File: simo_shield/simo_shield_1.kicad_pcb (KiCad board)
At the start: 2 copper layers, 70 x 100 mm, 10 parts, among them J1 modulo_usb_debug, J2 conector_bateria, U1 elemon_board, U2 modulo_flash_externa, U3 bluepill_board_stm32, U4 modulo_acelerometro

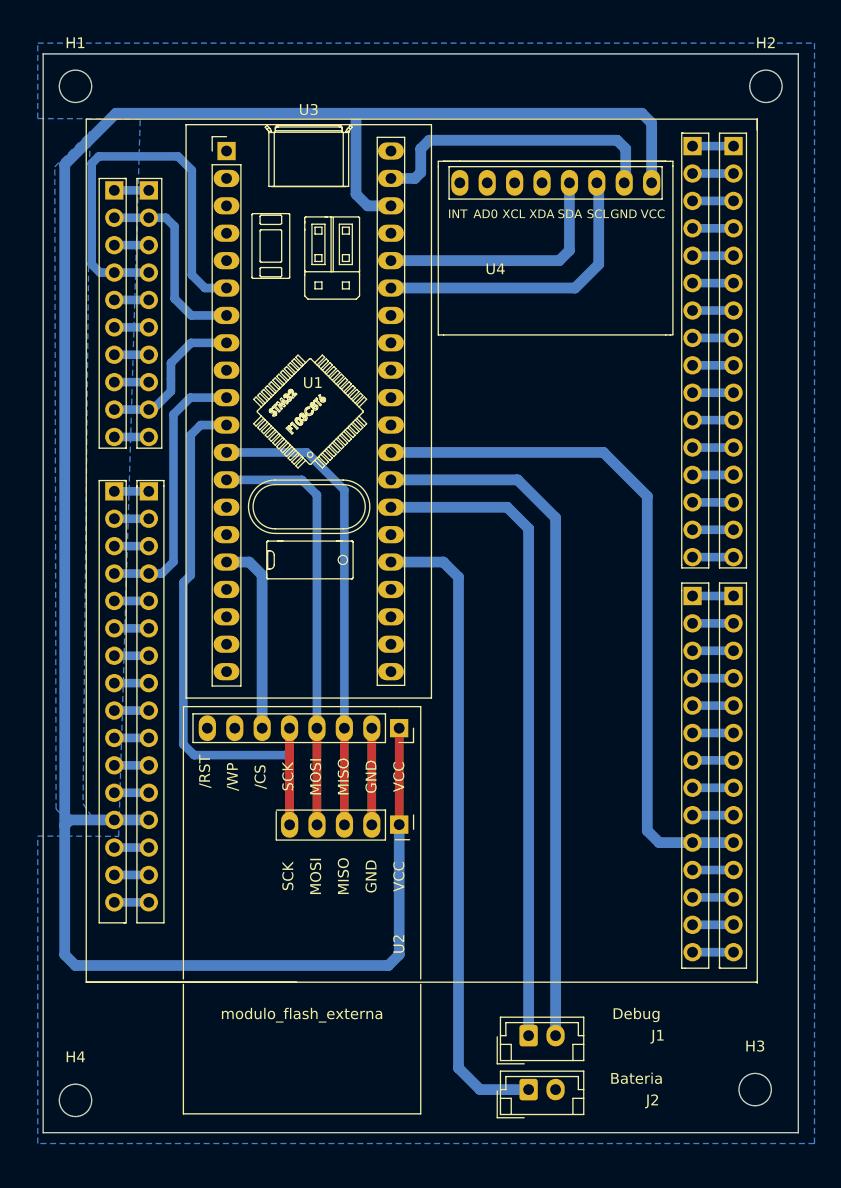
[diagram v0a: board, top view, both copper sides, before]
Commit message: modificaciones en simo shield:Se modificaron los planos para  enderezar los planos y se pulio detalles
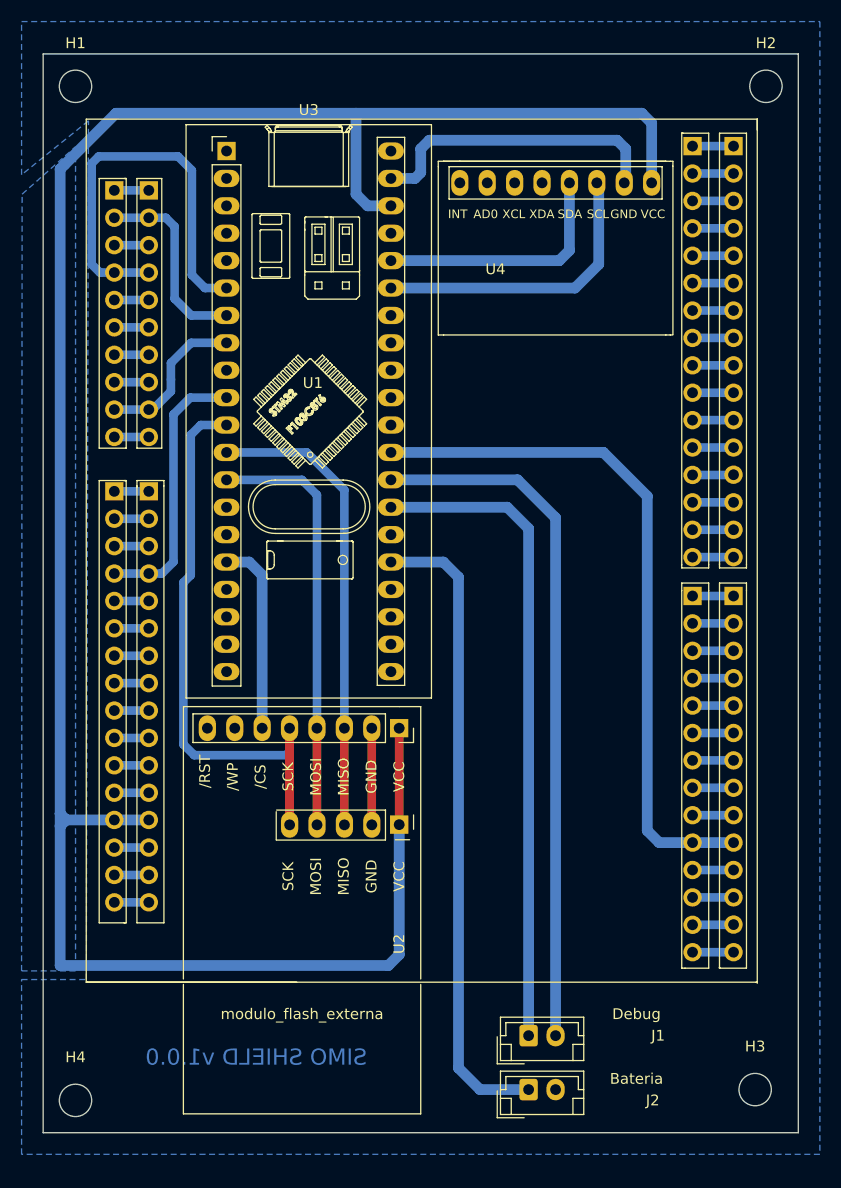
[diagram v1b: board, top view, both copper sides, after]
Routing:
- net /USB33_ELEMON: track 207.6 -> 210.0 mm
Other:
- board text added: "SIMO SHIELD v1.0.0"

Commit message: modificaciones simo shield: esquema y PCB. Detalle: se modifico la alimentacion y  eliminaron conectores custom
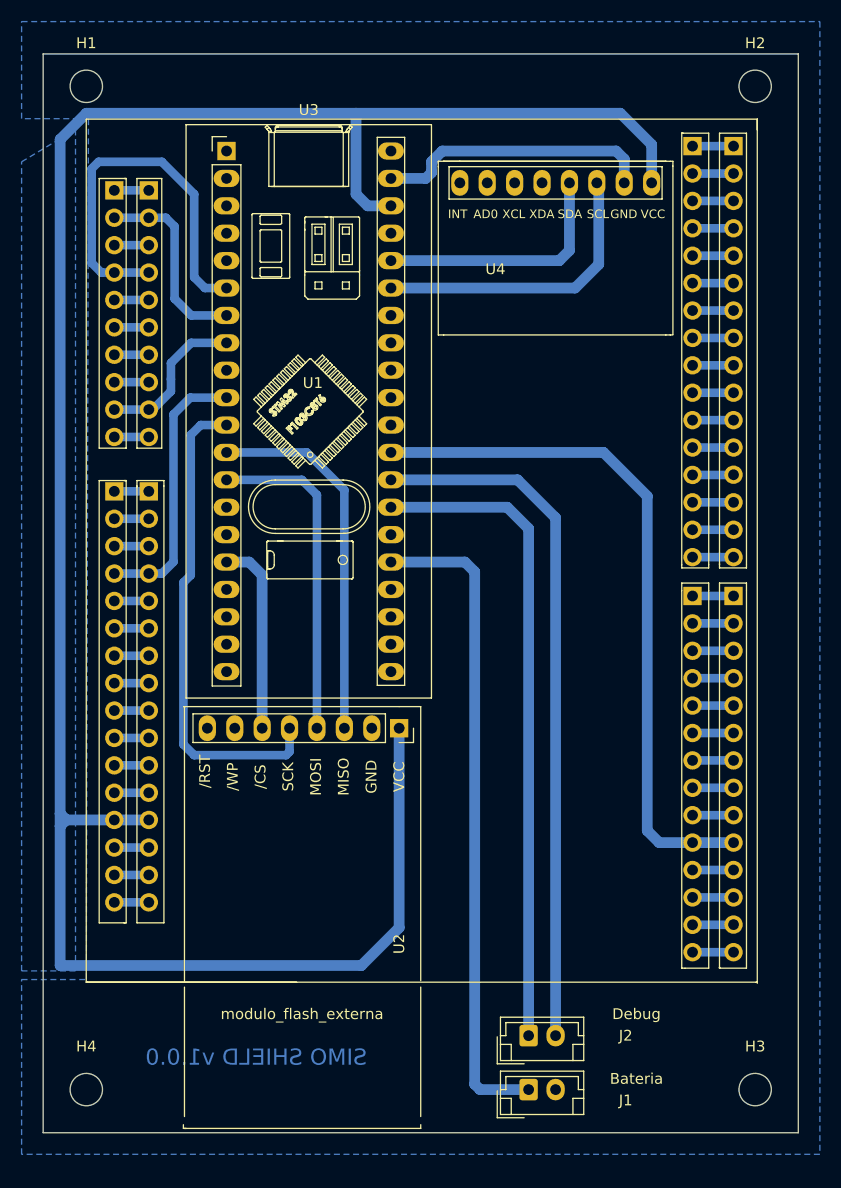
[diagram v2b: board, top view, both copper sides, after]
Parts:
- J1: value modulo_usb_debug -> Conn_01x02_Female
- J2: value conector_bateria -> Conn_01x02_Female
- moved J1 5.00 mm to (156.0, 123.0)
- moved J2 5.00 mm to (156.0, 118.0)
- moved H4 1.41 mm to (115.0, 123.0)
- moved H1 1.00 mm to (115.0, 30.0)
- moved H2 1.00 mm to (177.0, 30.0)
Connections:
- net /USB33_ELEMON renamed +3.3V
- J1 pad 1: /UART_DEBUG_RX -> Net-(U3-Pad25)
- J1 pad 2: /UART_DEBUG_TX -> GND
- J2 pad 1: Net-(J2-Pad1) -> /UART_DEBUG_RX
- J2 pad 2: /GND_ELEMON -> /UART_DEBUG_TX
- U1 pad 10: /BAT_GND -> unconnected-(U1-Pad10)
- U1 pad 24: /GND_ELEMON -> GND
- U2 pad 2: /GND_ELEMON -> GND
- U3 pad 25: Net-(J2-Pad1) -> Net-(U3-Pad25)
- U3 pad 39: /GND_ELEMON -> GND
- U4 pad 7: /GND_ELEMON -> GND
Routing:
- net Net-(U3-Pad25): track 0.00 -> 60.8 mm
- net Net-(J2-Pad1): track 59.7 -> 0.00 mm
- net /GND_ELEMON: track 40.2 -> 0.00 mm
- net GND: track 0.00 -> 29.0 mm
- net Net-(U2-Pad4): track 39.5 -> 30.6 mm
- net Net-(U2-Pad3): track 43.4 -> 34.4 mm
- net Net-(U2-Pad5): track 54.2 -> 45.2 mm
- net unconnected-(U1-Pad10): track 0.00 -> 3.20 mm
- net /BAT_GND: track 3.20 -> 0.00 mm
- net Net-(U1-Pad4): track 38.5 -> 36.5 mm
- net +3.3V: track 210.0 -> 209.0 mm
- added copper zone on B.Cu, net GND
- removed copper zone on B.Cu, net /GND_ELEMON

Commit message: update simo_shield:pcb
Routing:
- net +3.3V: track 209.0 -> 201.4 mm
- net /BAT_ENA_PIN: track 64.9 -> 60.2 mm
- net /UART_DEBUG_TX: track 64.7 -> 60.3 mm
- net /UART_DEBUG_RX: track 60.6 -> 56.5 mm
- net Net-(U3-Pad35): track 27.8 -> 24.9 mm
- net Net-(U3-Pad25): track 60.8 -> 57.9 mm
- net Net-(U2-Pad3): track 34.4 -> 31.7 mm
- net Net-(U3-Pad36): track 23.2 -> 20.9 mm
- net Net-(U2-Pad4): track 30.6 -> 28.2 mm
- net Net-(U1-Pad4): track 36.5 -> 38.1 mm
- net Net-(U2-Pad5): track 45.2 -> 44.1 mm
- net Net-(U1-Pad14): track 25.2 -> 24.3 mm
- net Net-(U1-Pad2): track 18.1 -> 17.3 mm
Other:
- board text added: "Fabrica: Metodo artesanal de planchado."
- board text added: "Grillas utilizadas: 1 mm Posicionamiento y ruteo 0,5 mm Ruteo fino 0,05 mm Plano VCC Ancho de pistas utilizadas: 1 mm Alimentacion 0,8 mm Resto de conexiones digitales Bordes del PCB: 1mm"

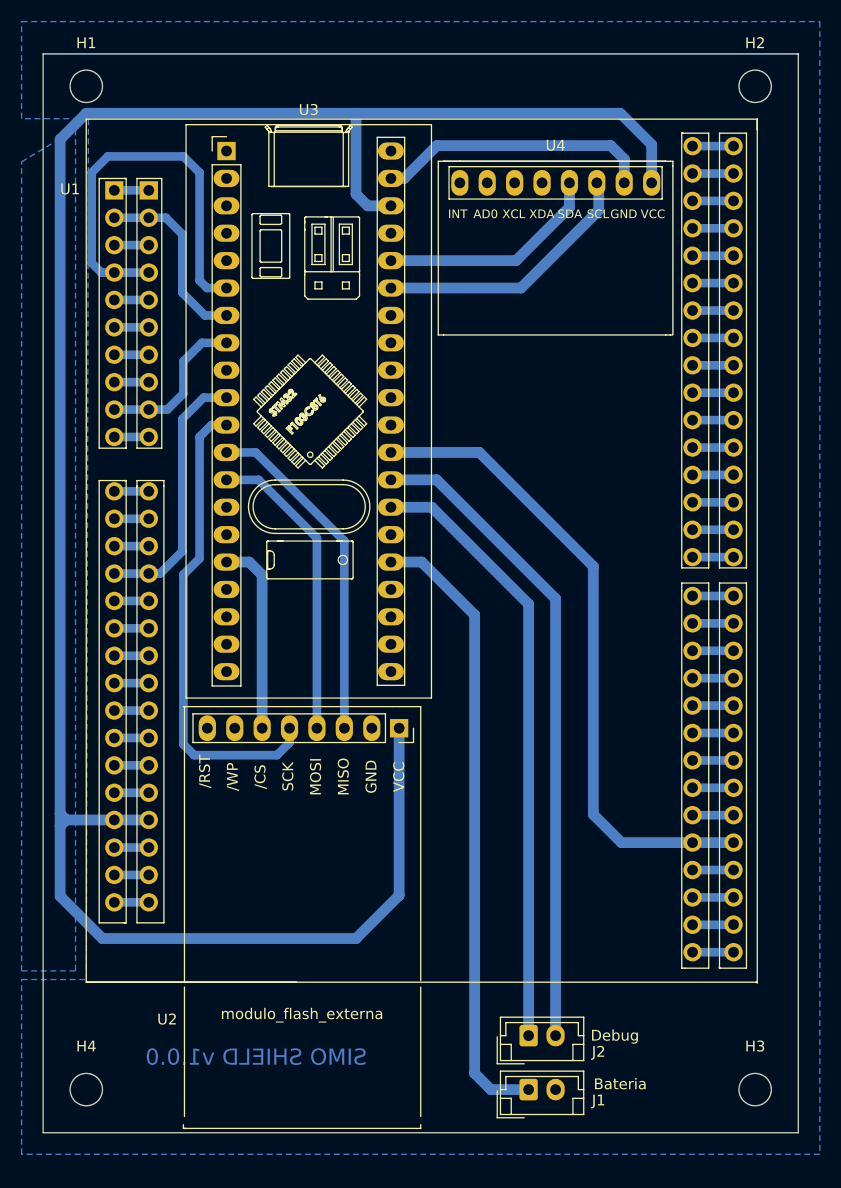
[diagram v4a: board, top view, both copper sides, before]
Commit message: Corregidos detalles en plano de Vcc y eliminada pista de GND en pin 39 del Bluepill.
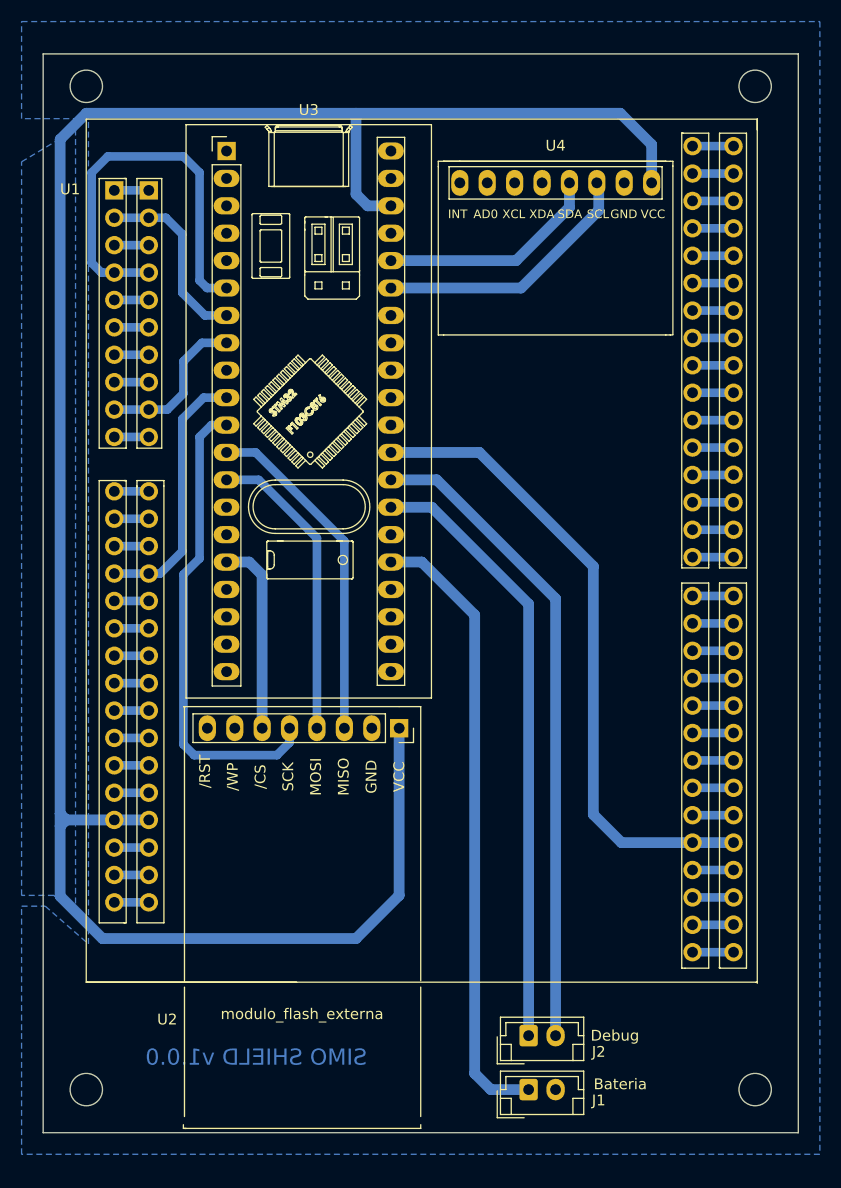
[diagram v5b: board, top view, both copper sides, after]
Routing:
- net GND: track 28.8 -> 3.20 mm

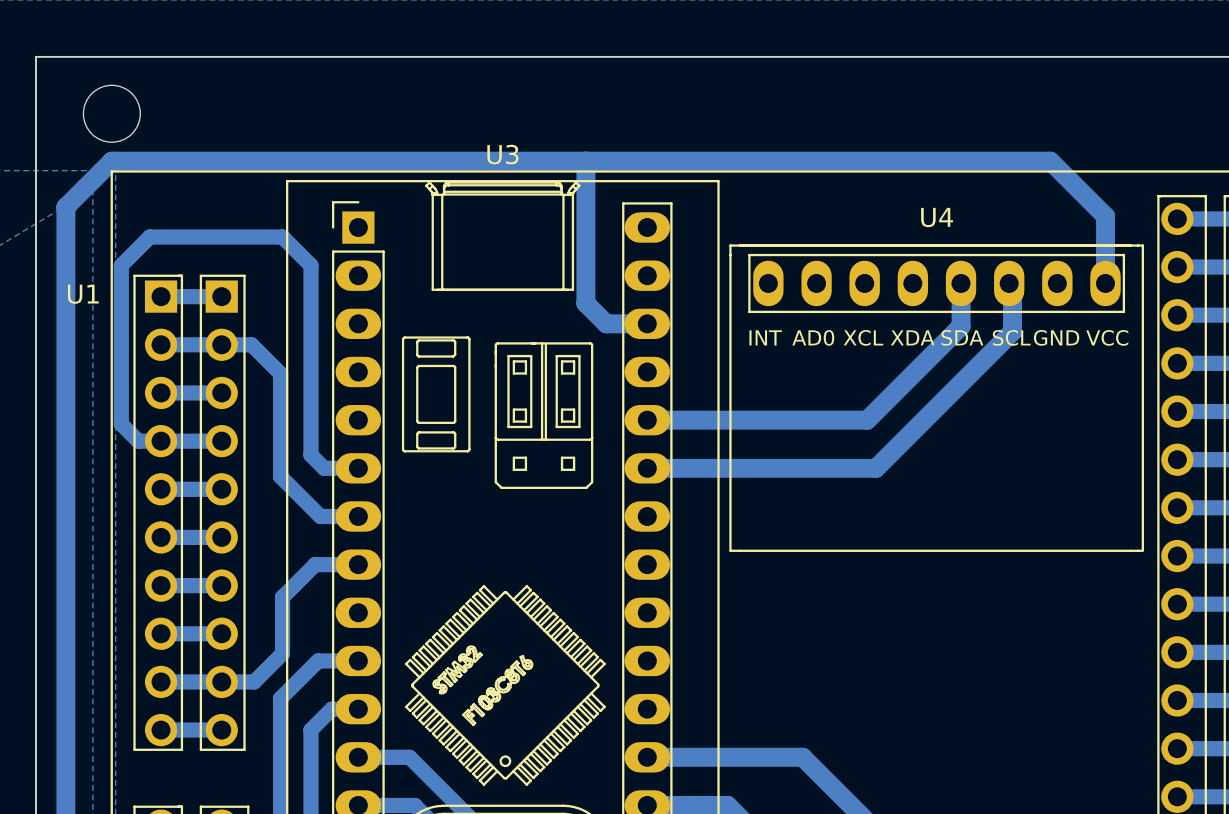
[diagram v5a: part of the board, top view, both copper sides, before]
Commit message: update: PINB13 paso a ser PA12. Modificar en firmware
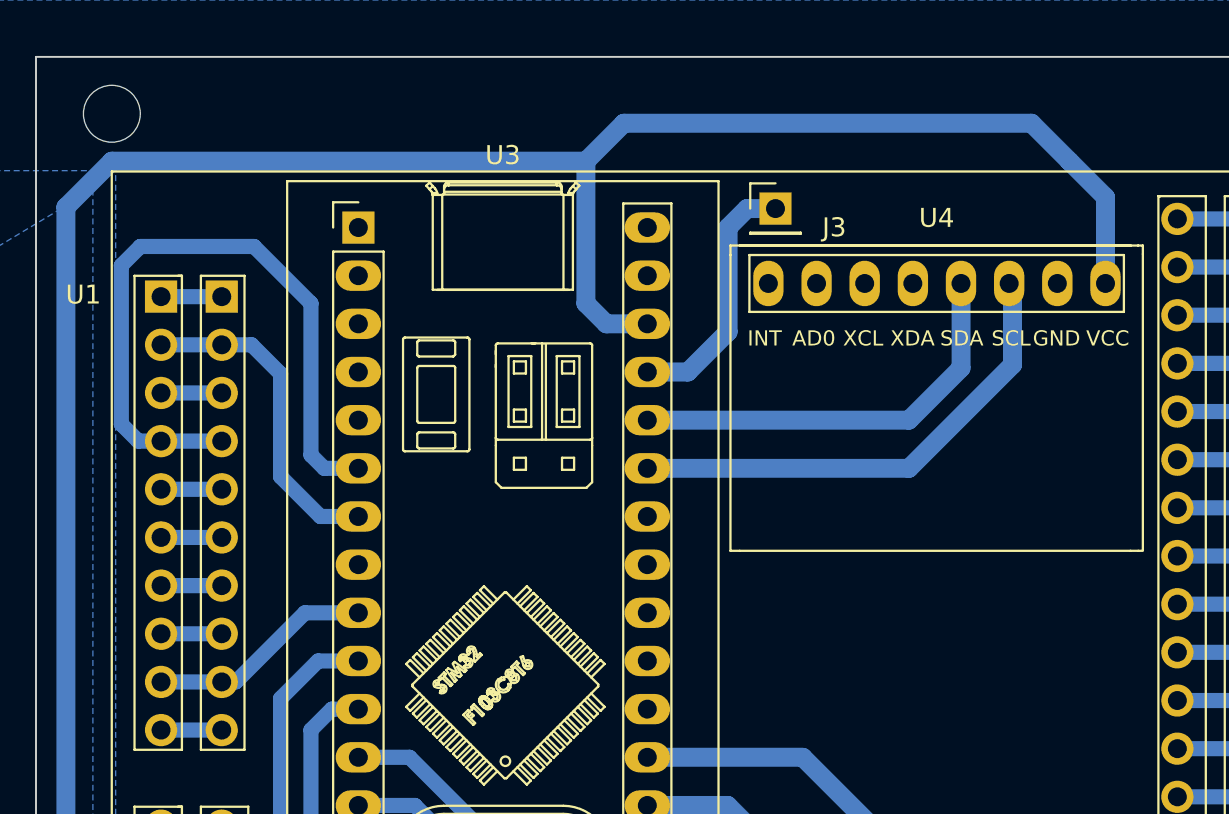
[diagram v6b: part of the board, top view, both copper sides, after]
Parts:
- added J3: Conn_01x01_Female, Connector_PinHeader_2.54mm:PinHeader_1x01_P2.54mm_Vertical, F.Cu at (150.0, 35.0)
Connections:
- U3 pad 37: unconnected-(U3-Pad37) -> Net-(J3-Pad1)
- U3 pad 8: Net-(U1-Pad9) -> unconnected-(U3-Pad8)
- U3 pad 9: unconnected-(U3-Pad9) -> Net-(U1-Pad9)
- U4 pad 7: GND -> +3.3V
- U4 pad 8: +3.3V -> GND
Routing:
- net Net-(J3-Pad1): track 0.00 -> 13.6 mm
- net Net-(U1-Pad9): track 14.7 -> 11.9 mm
- net +3.3V: track 201.4 -> 203.6 mm
- net Net-(U1-Pad4): track 38.1 -> 36.5 mm
- net Net-(U3-Pad36): track 20.9 -> 22.1 mm
- net Net-(U3-Pad35): track 24.9 -> 25.9 mm

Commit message: update pcb
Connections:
- U4 pad 7: +3.3V -> GND
- U4 pad 8: GND -> +3.3V
